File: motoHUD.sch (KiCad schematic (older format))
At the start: 120 parts, among them J1 POWER, J2 THERM1, J3 THERM2, J4 HALL, J5 SIG_RPM, J6 SIGNAL, J7 USB_B_Mini, J8 ICSP, J9 LCD Connector, M1 X27 168, Q1 2N7002KQ-13, Q2 2N7002KQ-13, SW1 TACTM-613N-F, U1 STM32F103C8Tx, U2 LM2904DT, U3 LM2904DT, U4 AZ1117-3.3, U5 MCP16301, U6 M95320-WMN6P, Y1 HC49USM-FF3F18-8M, Y2 LFXTAL009678

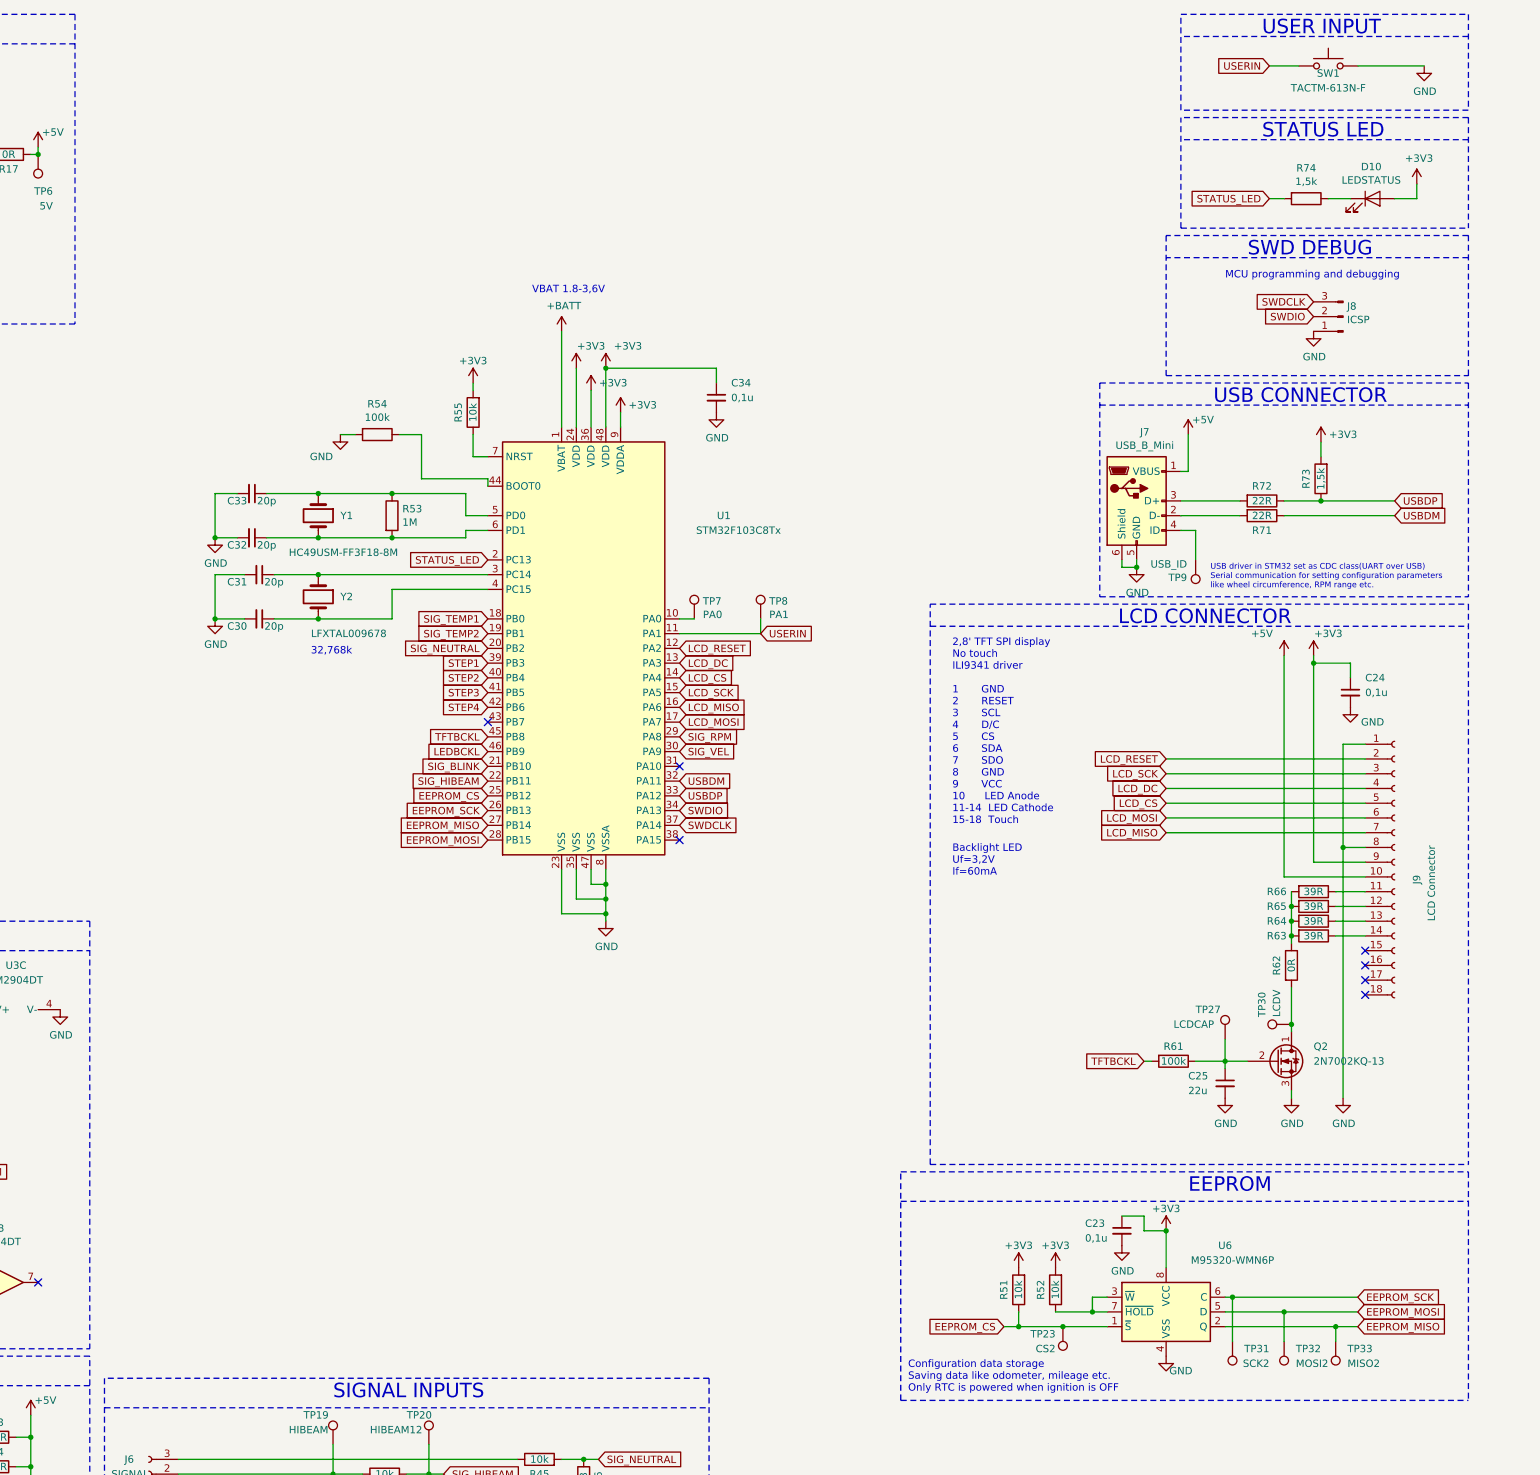
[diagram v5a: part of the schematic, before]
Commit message: 2nd button switch added and routed PCB
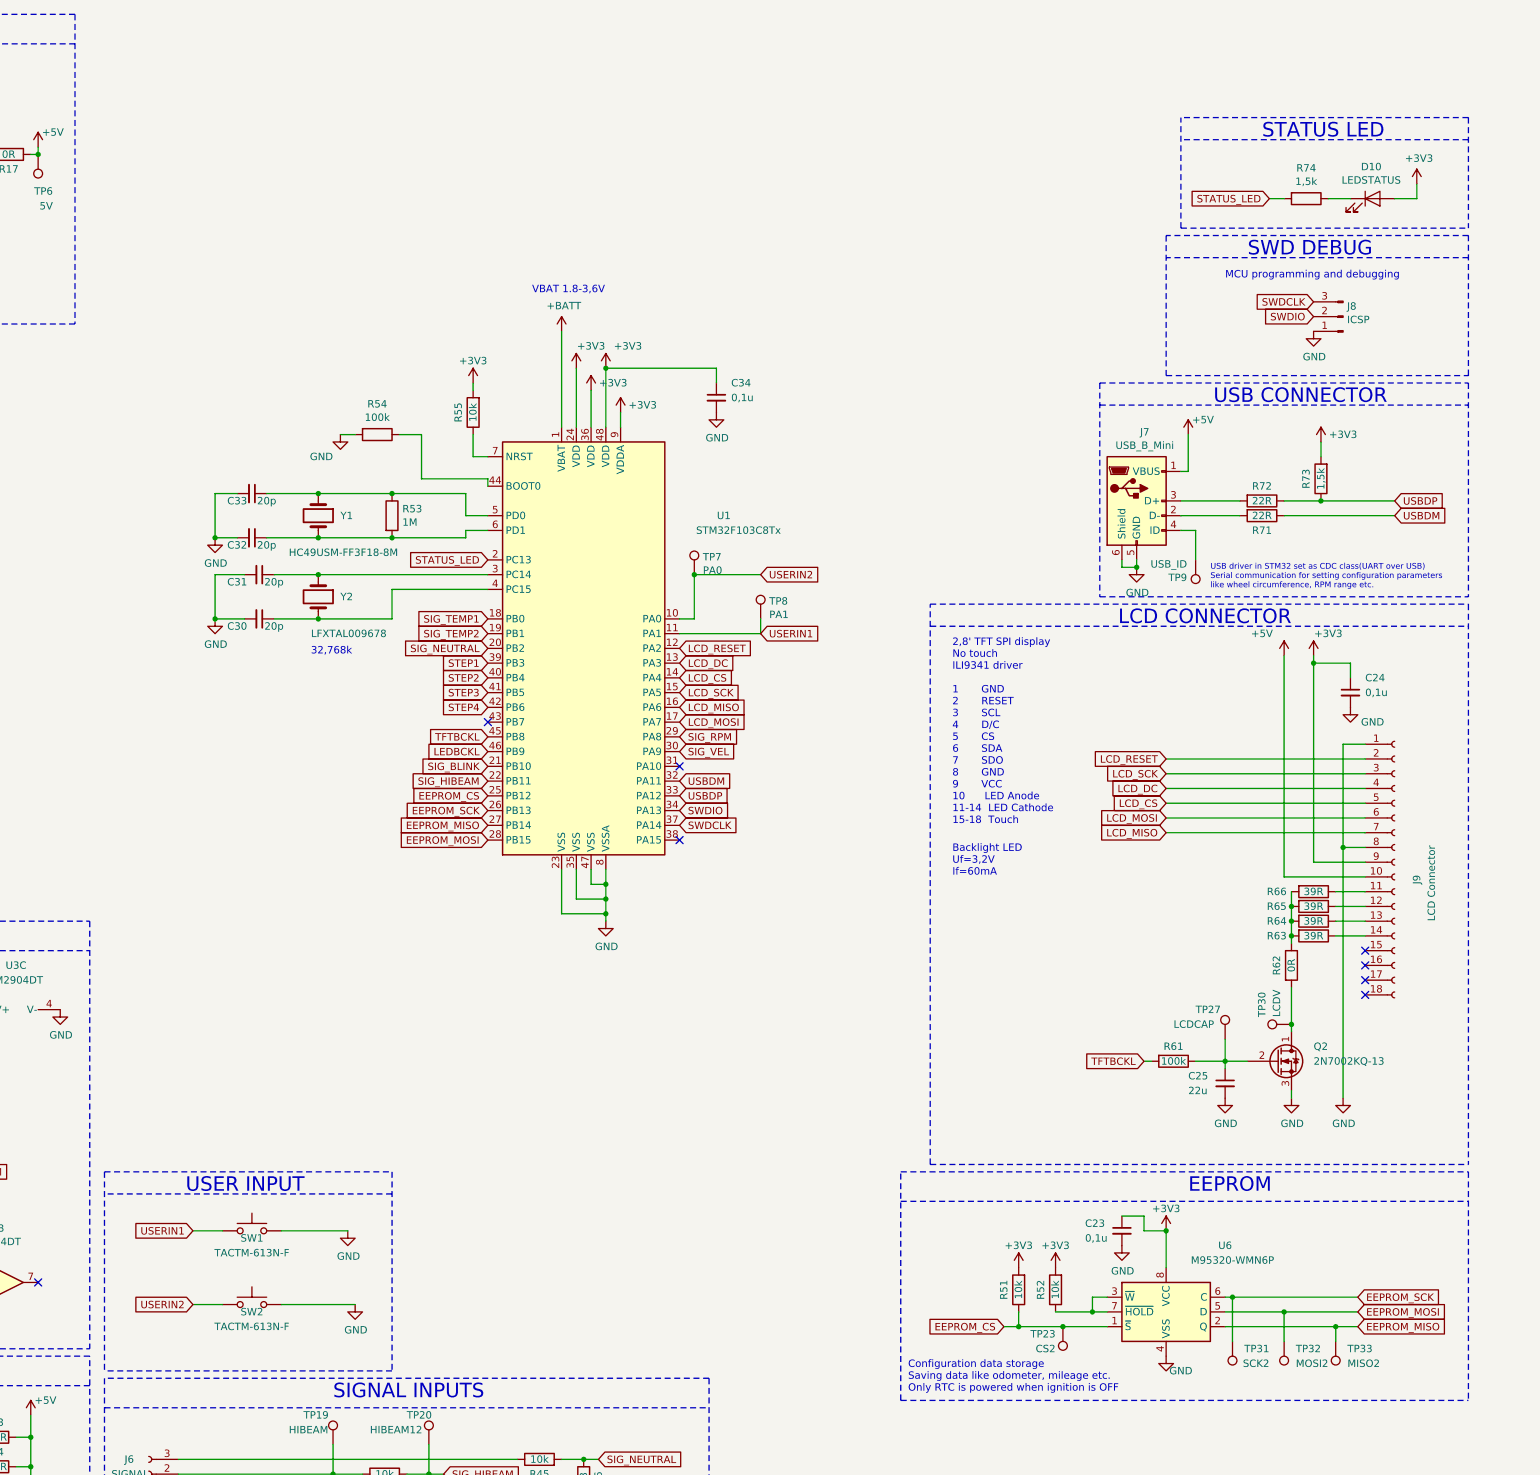
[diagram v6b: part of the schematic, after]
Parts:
- added SW2: TACTM-613N-F, motoHUD:TACTM-613N-F, symbol Switch:SW_Push
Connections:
- net GND: now also SW2.2
- net USERIN2: now reaches TP7.1, U1.10 (PA0)
- net USERIN2: now also SW2.1
- net USERIN renamed USERIN1
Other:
- moved on the sheet: SW1, TP7
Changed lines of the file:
@@
 L Connector:TestPoint TP7
 U 1 1 5D5733F6
-P 10750 4600
-F 0 "TP7" H 10808 4720 50  0000 L CNN
-F 1 "PA0" H 10808 4629 50  0000 L CNN
-F 2 "motoHUD:TestPoint_THTPad_D2.5mm_Drill1.2mm" H 10950 4600 50  0001 C CNN
-F 3 "" H 10950 4600 50  0001 C CNN
-	1    10750 4600
+P 10750 4300
+F 0 "TP7" H 10808 4420 50  0000 L CNN
+F 1 "PA0" H 10808 4329 50  0000 L CNN
+F 2 "motoHUD:TestPoint_THTPad_D2.5mm_Drill1.2mm" H 10950 4300 50  0001 C CNN
+F 3 "" H 10950 4300 50  0001 C CNN
+	1    10750 4300
 	1    0    0    -1
 $EndComp
@@
 Connection ~ 6300 1450
 Text GLabel 11200 4700 2    50   Input ~ 0
-USERIN
+USERIN1
 Wire Notes Line
 	16000 1200 16000 1950
@@
 L Switch:SW_Push SW1
 U 1 1 5DA294A1
-P 15050 850
-F 0 "SW1" H 15050 800 50  0000 C CNN
-F 1 "TACTM-613N-F" H 15050 700 50  0000 C CNN
-F 2 "motoHUD:TACTM-613N-F" H 15050 1050 50  0001 C CNN
-F 3 "https://www.tme.eu/pl/details/tactm-613n-f/mikroprzelaczniki-tact/ninigi/" H 15050 1050 50  0001 C CNN
-	1    15050 850
+P 7750 8750
+F 0 "SW1" H 7750 8700 50  0000 C CNN
+F 1 "TACTM-613N-F" H 7750 8600 50  0000 C CNN
+F 2 "motoHUD:TACTM-613N-F" H 7750 8950 50  0001 C CNN
+F 3 "https://www.tme.eu/pl/details/tactm-613n-f/mikroprzelaczniki-tact/ninigi/" H 7750 8950 50  0001 C CNN
+	1    7750 8750
 	1    0    0    -1
 $EndComp
@@
 L power:GND #PWR070
 U 1 1 5DA2A3A3
-P 15700 850
-F 0 "#PWR070" H 15700 600 50  0001 C CNN
-F 1 "GND" H 15705 677 50  0000 C CNN
-F 2 "" H 15700 850 50  0001 C CNN
-F 3 "" H 15700 850 50  0001 C CNN
-	1    15700 850
-	1    0    0    -1
-$EndComp
-Text GLabel 14650 850  0    50   Input ~ 0
-USERIN
-Wire Wire Line
-	15700 850  15250 850
-Wire Wire Line
-	14850 850  14650 850
-Wire Notes Line
-	16000 1150 14050 1150
-Wire Notes Line
-	14050 1150 14050 500
-Wire Notes Line
-	14050 500  16000 500
-Wire Notes Line
-	16000 500  16000 1150
-Wire Notes Line
-	16000 650  14050 650
-Text Notes 14600 650  0    98   ~ 0
+P 8400 8750
+F 0 "#PWR070" H 8400 8500 50  0001 C CNN
+F 1 "GND" H 8405 8577 50  0000 C CNN
+F 2 "" H 8400 8750 50  0001 C CNN
+F 3 "" H 8400 8750 50  0001 C CNN
+	1    8400 8750
+	1    0    0    -1
+$EndComp
+Text GLabel 7350 8750 0    50   Input ~ 0
+USERIN1
+Wire Wire Line
+	8400 8750 7950 8750
+Wire Wire Line
+	7550 8750 7350 8750
+Wire Notes Line
+	6750 8350 8700 8350
+Wire Notes Line
+	8700 8500 6750 8500
+Text Notes 7300 8500 0    98   ~ 0
 USER INPUT
 Wire Notes Line
@@
 Wire Wire Line
 	13950 5850 15300 5850
+Text GLabel 11200 4300 2    50   Input ~ 0
+USERIN2
+Wire Wire Line
+	10750 4600 10750 4300
+Wire Wire Line
+	11200 4300 10750 4300
+Connection ~ 10750 4300
+Text GLabel 7350 9250 0    50   Input ~ 0
+USERIN2
+$Comp
+L Switch:SW_Push SW2
+U 1 1 5DA9863F
+P 7750 9250
+F 0 "SW2" H 7750 9200 50  0000 C CNN
+F 1 "TACTM-613N-F" H 7750 9100 50  0000 C CNN
+F 2 "motoHUD:TACTM-613N-F" H 7750 9450 50  0001 C CNN
+F 3 "https://www.tme.eu/pl/details/tactm-613n-f/mikroprzelaczniki-tact/ninigi/" H 7750 9450 50  0001 C CNN
+	1    7750 9250
+	1    0    0    -1
+$EndComp
+$Comp
+L power:GND #PWR071
+U 1 1 5DA98759
+P 8450 9250
+F 0 "#PWR071" H 8450 9000 50  0001 C CNN
+F 1 "GND" H 8455 9077 50  0000 C CNN
+F 2 "" H 8450 9250 50  0001 C CNN
+F 3 "" H 8450 9250 50  0001 C CNN
+	1    8450 9250
+	1    0    0    -1
+$EndComp
+Wire Wire Line
+	8450 9250 7950 9250
+Wire Wire Line
+	7550 9250 7350 9250
+Wire Notes Line
+	8700 9700 6750 9700
+Wire Notes Line
+	6750 8350 6750 9700
+Wire Notes Line
+	8700 8350 8700 9700
 $EndSCHEMATC

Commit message: PCB design improvements
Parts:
- TP1, TP10, TP11, TP12, TP13, TP14, TP15, TP16, TP19, TP2, TP20, TP23, TP27, TP3, TP30, TP31, TP32, TP33, TP4, TP5, TP6, TP7, TP8, TP9: footprint motoHUD:TestPoint_THTPad_D2.5mm_Drill1.2mm -> TestPoint:TestPoint_THTPad_D2.0mm_Drill1.0mm
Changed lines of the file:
@@
 F 0 "TP9" H 14208 4320 50  0000 L CNN
 F 1 "USB_ID" H 14208 4229 50  0000 L CNN
-F 2 "motoHUD:TestPoint_THTPad_D2.5mm_Drill1.2mm" H 14350 4200 50  0001 C CNN
+F 2 "TestPoint:TestPoint_THTPad_D2.0mm_Drill1.0mm" H 14350 4200 50  0001 C CNN
 F 3 "" H 14350 4200 50  0001 C CNN
 	1    14150 4200
@@
 F 0 "TP5" H 3758 10470 50  0000 L CNN
 F 1 "BCKL_CAP" H 3758 10379 50  0000 L CNN
-F 2 "motoHUD:TestPoint_THTPad_D2.5mm_Drill1.2mm" H 3900 10350 50  0001 C CNN
+F 2 "TestPoint:TestPoint_THTPad_D2.0mm_Drill1.0mm" H 3900 10350 50  0001 C CNN
 F 3 "" H 3900 10350 50  0001 C CNN
 	1    3700 10350
@@
 F 0 "TP3" H 2550 2000 50  0000 L CNN
 F 1 "V_RTC" H 2500 2100 50  0000 L CNN
-F 2 "motoHUD:TestPoint_THTPad_D2.5mm_Drill1.2mm" H 2800 1800 50  0001 C CNN
+F 2 "TestPoint:TestPoint_THTPad_D2.0mm_Drill1.0mm" H 2800 1800 50  0001 C CNN
 F 3 "" H 2800 1800 50  0001 C CNN
 	1    2600 1800
@@
 F 0 "TP7" H 10808 4420 50  0000 L CNN
 F 1 "PA0" H 10808 4329 50  0000 L CNN
-F 2 "motoHUD:TestPoint_THTPad_D2.5mm_Drill1.2mm" H 10950 4300 50  0001 C CNN
+F 2 "TestPoint:TestPoint_THTPad_D2.0mm_Drill1.0mm" H 10950 4300 50  0001 C CNN
 F 3 "" H 10950 4300 50  0001 C CNN
 	1    10750 4300
@@
 F 0 "TP8" H 11258 4720 50  0000 L CNN
 F 1 "PA1" H 11258 4629 50  0000 L CNN
-F 2 "motoHUD:TestPoint_THTPad_D2.5mm_Drill1.2mm" H 11400 4600 50  0001 C CNN
+F 2 "TestPoint:TestPoint_THTPad_D2.0mm_Drill1.0mm" H 11400 4600 50  0001 C CNN
 F 3 "" H 11400 4600 50  0001 C CNN
 	1    11200 4600
@@
 F 0 "TP4" H 3300 1550 50  0000 L CNN
 F 1 "V_IGN" H 3250 1650 50  0000 L CNN
-F 2 "motoHUD:TestPoint_THTPad_D2.5mm_Drill1.2mm" H 3550 1350 50  0001 C CNN
+F 2 "TestPoint:TestPoint_THTPad_D2.0mm_Drill1.0mm" H 3550 1350 50  0001 C CNN
 F 3 "" H 3550 1350 50  0001 C CNN
 	1    3350 1350
@@
 F 0 "TP6" H 6200 1700 50  0000 L CNN
 F 1 "5V" H 6200 1800 50  0000 L CNN
-F 2 "motoHUD:TestPoint_THTPad_D2.5mm_Drill1.2mm" H 6500 1450 50  0001 C CNN
+F 2 "TestPoint:TestPoint_THTPad_D2.0mm_Drill1.0mm" H 6500 1450 50  0001 C CNN
 F 3 "" H 6500 1450 50  0001 C CNN
 	1    6300 1450
@@
 F 0 "TP2" H 2500 4950 50  0000 L CNN
 F 1 "3v3" H 2450 5050 50  0000 L CNN
-F 2 "motoHUD:TestPoint_THTPad_D2.5mm_Drill1.2mm" H 2750 4750 50  0001 C CNN
+F 2 "TestPoint:TestPoint_THTPad_D2.0mm_Drill1.0mm" H 2750 4750 50  0001 C CNN
 F 3 "" H 2750 4750 50  0001 C CNN
 	1    2550 4750
@@
 F 0 "TP1" H 1150 6550 50  0000 L CNN
 F 1 "VEL" H 1100 6650 50  0000 L CNN
-F 2 "motoHUD:TestPoint_THTPad_D2.5mm_Drill1.2mm" H 1400 6350 50  0001 C CNN
+F 2 "TestPoint:TestPoint_THTPad_D2.0mm_Drill1.0mm" H 1400 6350 50  0001 C CNN
 F 3 "~" H 1400 6350 50  0001 C CNN
 	1    1200 6350
@@
 F 0 "TP10" H 1350 9450 50  0000 L CNN
 F 1 "TEMP1" H 1300 9550 50  0000 L CNN
-F 2 "motoHUD:TestPoint_THTPad_D2.5mm_Drill1.2mm" H 1600 9250 50  0001 C CNN
+F 2 "TestPoint:TestPoint_THTPad_D2.0mm_Drill1.0mm" H 1600 9250 50  0001 C CNN
 F 3 "~" H 1600 9250 50  0001 C CNN
 	1    1400 9250
@@
 F 0 "TP11" H 1350 10700 50  0000 L CNN
 F 1 "TEMP2" H 1300 10800 50  0000 L CNN
-F 2 "motoHUD:TestPoint_THTPad_D2.5mm_Drill1.2mm" H 1600 10500 50  0001 C CNN
+F 2 "TestPoint:TestPoint_THTPad_D2.0mm_Drill1.0mm" H 1600 10500 50  0001 C CNN
 F 3 "~" H 1600 10500 50  0001 C CNN
 	1    1400 10500
@@
 F 0 "TP12" H 4100 8400 50  0000 L CNN
 F 1 "RPMA" H 4050 8500 50  0000 L CNN
-F 2 "motoHUD:TestPoint_THTPad_D2.5mm_Drill1.2mm" H 4350 8200 50  0001 C CNN
+F 2 "TestPoint:TestPoint_THTPad_D2.0mm_Drill1.0mm" H 4350 8200 50  0001 C CNN
 F 3 "~" H 4350 8200 50  0001 C CNN
 	1    4150 8200
@@
 F 0 "TP16" H 5500 8550 50  0000 L CNN
 F 1 "RPMD" H 5450 8650 50  0000 L CNN
-F 2 "motoHUD:TestPoint_THTPad_D2.5mm_Drill1.2mm" H 5750 8350 50  0001 C CNN
+F 2 "TestPoint:TestPoint_THTPad_D2.0mm_Drill1.0mm" H 5750 8350 50  0001 C CNN
 F 3 "~" H 5750 8350 50  0001 C CNN
 	1    5550 8350
@@
 F 0 "TP13" H 4100 1300 50  0000 L CNN
 F 1 "BOOST" H 4050 1200 50  0000 L CNN
-F 2 "motoHUD:TestPoint_THTPad_D2.5mm_Drill1.2mm" H 4550 1050 50  0001 C CNN
+F 2 "TestPoint:TestPoint_THTPad_D2.0mm_Drill1.0mm" H 4550 1050 50  0001 C CNN
 F 3 "" H 4550 1050 50  0001 C CNN
 	1    4350 1050
@@
 F 0 "TP15" H 4400 8300 50  0000 L CNN
 F 1 "RPMC" H 4200 8250 50  0000 L CNN
-F 2 "motoHUD:TestPoint_THTPad_D2.5mm_Drill1.2mm" H 4650 8100 50  0001 C CNN
+F 2 "TestPoint:TestPoint_THTPad_D2.0mm_Drill1.0mm" H 4650 8100 50  0001 C CNN
 F 3 "~" H 4650 8100 50  0001 C CNN
 	1    4450 8100
@@
 F 0 "TP14" H 4400 10350 50  0000 L CNN
 F 1 "BCKL_V" H 4400 10250 50  0000 L CNN
-F 2 "motoHUD:TestPoint_THTPad_D2.5mm_Drill1.2mm" H 4550 10150 50  0001 C CNN
+F 2 "TestPoint:TestPoint_THTPad_D2.0mm_Drill1.0mm" H 4550 10150 50  0001 C CNN
 F 3 "" H 4550 10150 50  0001 C CNN
 	1    4350 10150
@@
 F 0 "TP19" H 8100 10400 50  0000 L CNN
 F 1 "HIBEAM" H 8000 10300 50  0000 L CNN
-F 2 "motoHUD:TestPoint_THTPad_D2.5mm_Drill1.2mm" H 8500 10200 50  0001 C CNN
+F 2 "TestPoint:TestPoint_THTPad_D2.0mm_Drill1.0mm" H 8500 10200 50  0001 C CNN
 F 3 "" H 8500 10200 50  0001 C CNN
 	1    8300 10200
@@
 F 0 "TP20" H 8800 10400 50  0000 L CNN
 F 1 "HIBEAM12" H 8550 10300 50  0000 L CNN
-F 2 "motoHUD:TestPoint_THTPad_D2.5mm_Drill1.2mm" H 9150 10200 50  0001 C CNN
+F 2 "TestPoint:TestPoint_THTPad_D2.0mm_Drill1.0mm" H 9150 10200 50  0001 C CNN
 F 3 "" H 9150 10200 50  0001 C CNN
 	1    8950 10200
@@
 F 0 "TP27" H 14150 7650 50  0000 L CNN
 F 1 "LCDCAP" H 14000 7550 50  0000 L CNN
-F 2 "motoHUD:TestPoint_THTPad_D2.5mm_Drill1.2mm" H 14550 7450 50  0001 C CNN
+F 2 "TestPoint:TestPoint_THTPad_D2.0mm_Drill1.0mm" H 14550 7450 50  0001 C CNN
 F 3 "" H 14550 7450 50  0001 C CNN
 	1    14350 7450
@@
 F 0 "TP23" H 13300 9450 50  0000 L CNN
 F 1 "CS2" H 13300 9550 50  0000 L CNN
-F 2 "motoHUD:TestPoint_THTPad_D2.5mm_Drill1.2mm" H 13450 9400 50  0001 C CNN
+F 2 "TestPoint:TestPoint_THTPad_D2.0mm_Drill1.0mm" H 13450 9400 50  0001 C CNN
 F 3 "" H 13450 9400 50  0001 C CNN
 	1    13250 9400
@@
 F 0 "TP30" H 14850 7550 50  0000 L CNN
 F 1 "LCDV" H 14850 7450 50  0000 L CNN
-F 2 "motoHUD:TestPoint_THTPad_D2.5mm_Drill1.2mm" H 15000 7350 50  0001 C CNN
+F 2 "TestPoint:TestPoint_THTPad_D2.0mm_Drill1.0mm" H 15000 7350 50  0001 C CNN
 F 3 "" H 15000 7350 50  0001 C CNN
 	1    14800 7350
@@
 F 0 "TP31" H 14150 9550 50  0000 L CNN
 F 1 "SCK2" H 14150 9650 50  0000 L CNN
-F 2 "motoHUD:TestPoint_THTPad_D2.5mm_Drill1.2mm" H 14600 9500 50  0001 C CNN
+F 2 "TestPoint:TestPoint_THTPad_D2.0mm_Drill1.0mm" H 14600 9500 50  0001 C CNN
 F 3 "" H 14600 9500 50  0001 C CNN
 	1    14400 9500
@@
 F 0 "TP32" H 14500 9550 50  0000 L CNN
 F 1 "MOSI2" H 14450 9650 50  0000 L CNN
-F 2 "motoHUD:TestPoint_THTPad_D2.5mm_Drill1.2mm" H 14950 9500 50  0001 C CNN
+F 2 "TestPoint:TestPoint_THTPad_D2.0mm_Drill1.0mm" H 14950 9500 50  0001 C CNN
 F 3 "" H 14950 9500 50  0001 C CNN
 	1    14750 9500
@@
 F 0 "TP33" H 14850 9550 50  0000 L CNN
 F 1 "MISO2" H 14800 9650 50  0000 L CNN
-F 2 "motoHUD:TestPoint_THTPad_D2.5mm_Drill1.2mm" H 15300 9500 50  0001 C CNN
+F 2 "TestPoint:TestPoint_THTPad_D2.0mm_Drill1.0mm" H 15300 9500 50  0001 C CNN
 F 3 "" H 15300 9500 50  0001 C CNN
 	1    15100 9500
